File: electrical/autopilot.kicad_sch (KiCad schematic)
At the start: 5 parts

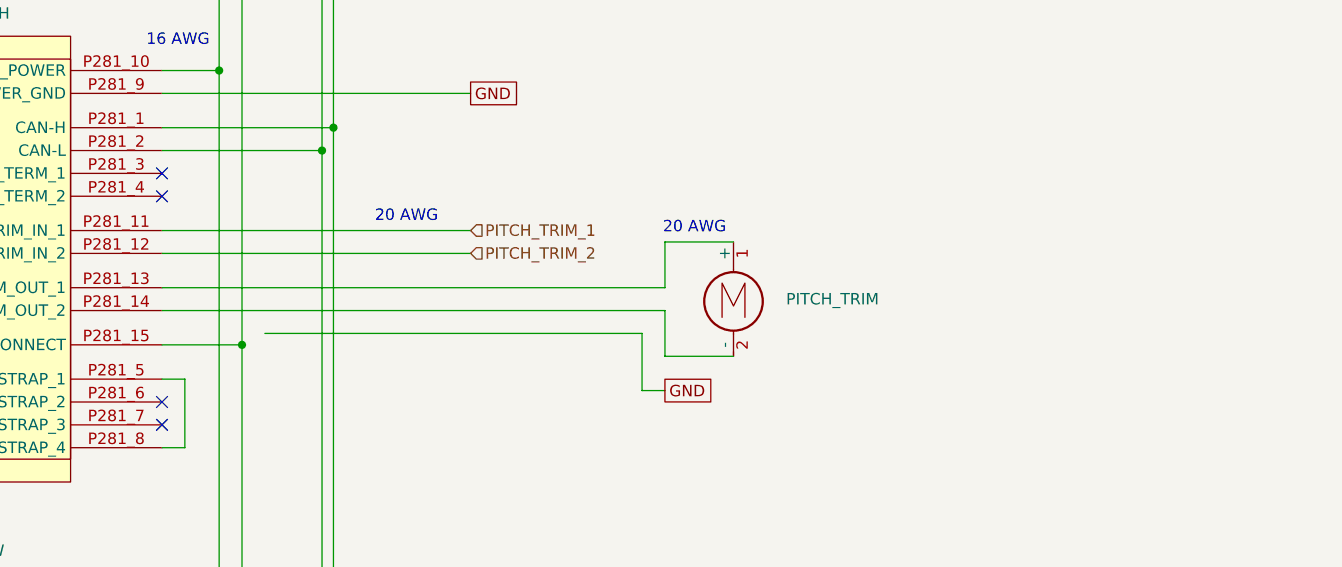
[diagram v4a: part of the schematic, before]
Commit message: Added Rudder Trim and Ray Allen T3 Servo Type.
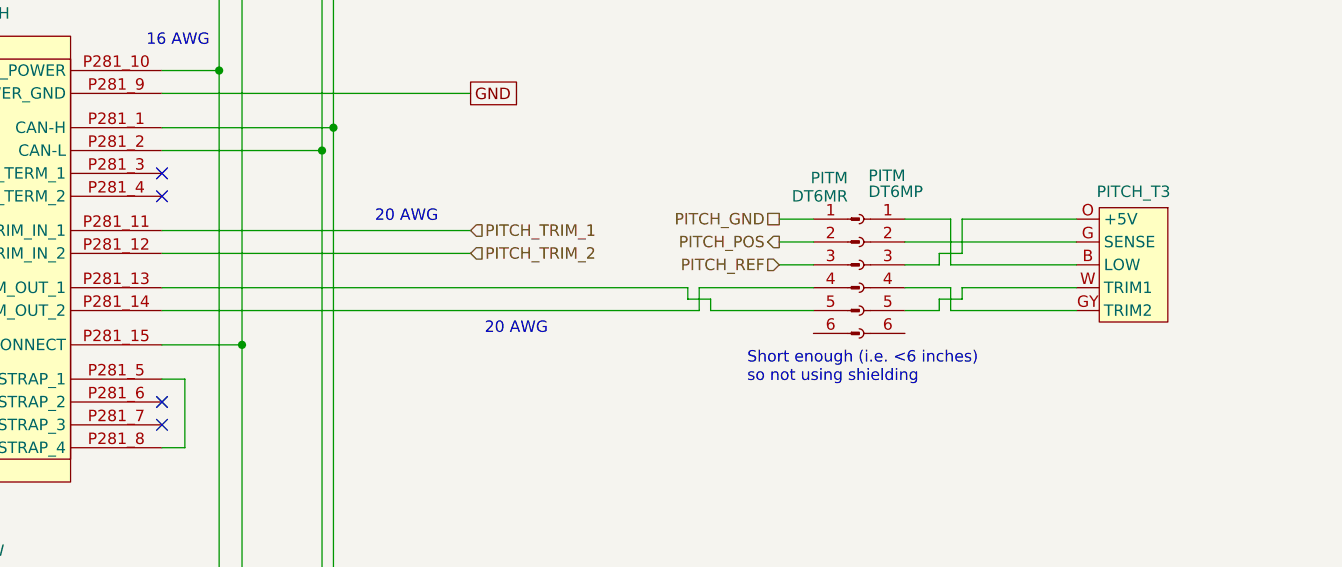
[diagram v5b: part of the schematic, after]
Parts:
- removed PITCH_TRIM: Motor_DC, symbol Motor:Motor_DC
- added PITCH_T3: ~, symbol flyerx:Ray_Allen_T2/T3
- added PITM: DT6MR, symbol Connector:Conn_01x06_Pin
- added PITM: DT6MP, symbol Connector:Conn_01x06_Socket
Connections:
- net at GSA28_PITCH.P281_13 (TRIM_OUT_1): now also PITM.5 (Pin_5)
- net at GSA28_PITCH.P281_14 (TRIM_OUT_2): now also PITM.4 (Pin_4)
- new net: PITCH_T3.B (LOW), PITM.1 (Pin_1)
- new net: PITCH_T3.G (SENSE), PITM.2 (Pin_2)
- new net: PITCH_T3.O (+5V), PITM.3 (Pin_3)
- new net: PITCH_T3.GY (TRIM2), PITM.4 (Pin_4)
- new net: PITCH_T3.W (TRIM1), PITM.5 (Pin_5)
- new net PITCH_GND: PITM.1 (Pin_1)
- new net PITCH_POS: PITM.2 (Pin_2)
- new net PITCH_REF: PITM.3 (Pin_3)
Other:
- note added: "Short enough (i.e. <6 inches) so not using shielding"

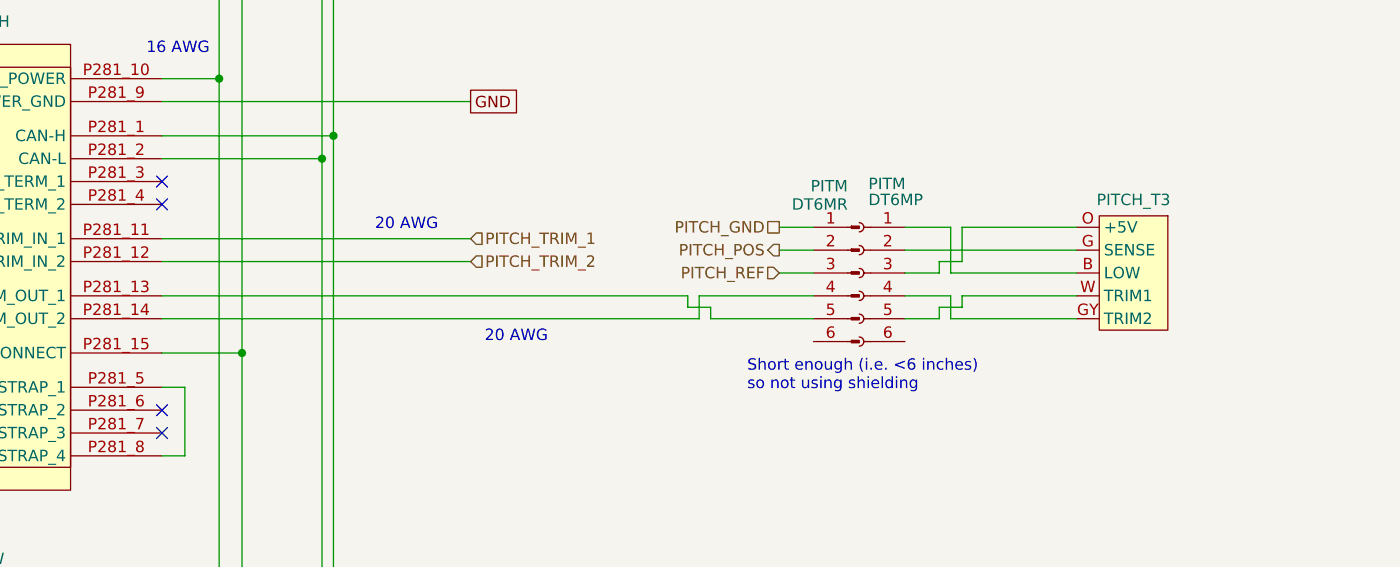
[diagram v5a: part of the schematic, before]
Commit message: Interim check-in getting colors correct.
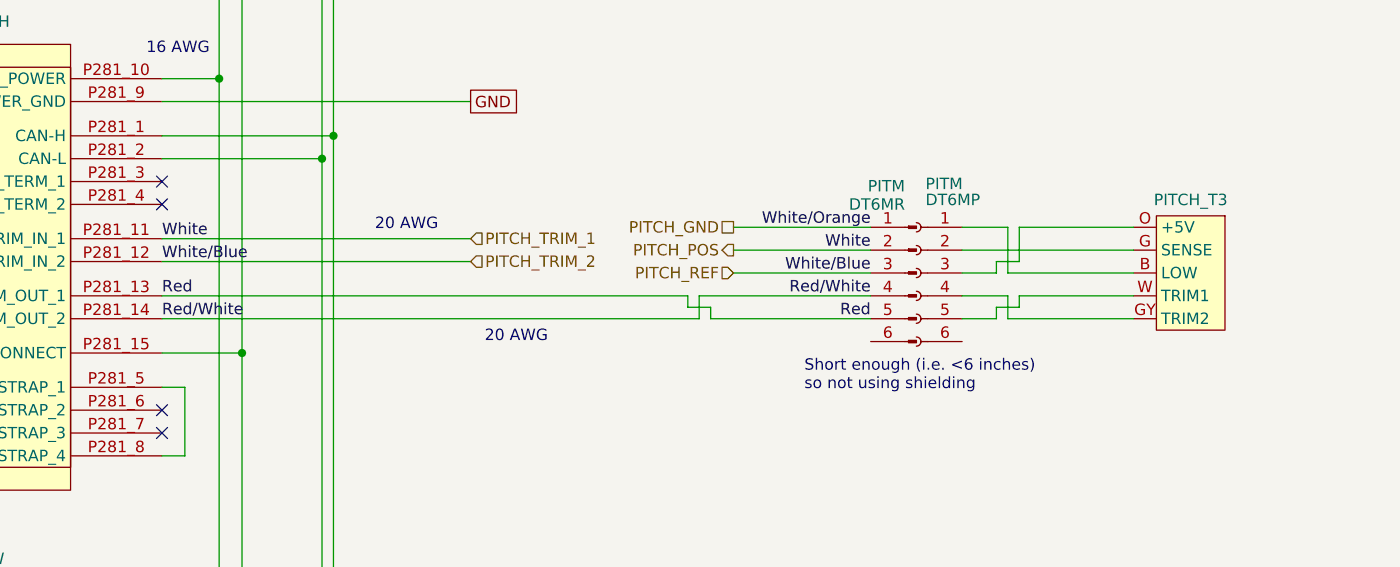
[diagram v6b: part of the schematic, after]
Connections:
- net PITCH_TRIM_1 is gone; now on net PITCH_POS: GSA28_PITCH.P281_11 (TRIM_IN_1)
- net PITCH_TRIM_2 is gone; now on net PITCH_REF: GSA28_PITCH.P281_12 (TRIM_IN_2)
- net Red/White: now reaches GSA28_PITCH.P281_14 (TRIM_OUT_2), PITM.4 (Pin_4)
- net Red: now reaches GSA28_PITCH.P281_13 (TRIM_OUT_1), PITM.5 (Pin_5)
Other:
- moved on the sheet: PITCH_T3, PITM
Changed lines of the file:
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@@
 	(text "Short enough (i.e. <6 inches)\nso not using shielding"
 		(exclude_from_sim no)
-		(at 120.904 119.38 0)
+		(at 127.254 119.38 0)
 		(effects
 			(font
@@
 	(wire
 		(pts
-			(xy 143.51 107.95) (xy 157.48 107.95)
-		)
-		(stroke
-			(width 0)
-			(type default)
-		)
-	)
-	(wire
-		(pts
-			(xy 138.43 110.49) (xy 143.51 110.49)
+			(xy 149.86 107.95) (xy 163.83 107.95)
+		)
+		(stroke
+			(width 0)
+			(type default)
+		)
+	)
+	(wire
+		(pts
+			(xy 144.78 110.49) (xy 149.86 110.49)
 		)
 		(stroke
@@
 	(wire
 		(pts
-			(xy 116.84 113.03) (xy 128.27 113.03)
+			(xy 116.84 113.03) (xy 134.62 113.03)
 		)
 		(stroke
@@
 	(wire
 		(pts
-			(xy 124.46 102.87) (xy 128.27 102.87)
+			(xy 119.38 102.87) (xy 134.62 102.87)
 		)
 		(stroke
@@
 	(wire
 		(pts
-			(xy 143.51 113.03) (xy 157.48 113.03)
+			(xy 149.86 113.03) (xy 163.83 113.03)
 		)
 		(stroke
@@
 	(wire
 		(pts
-			(xy 138.43 105.41) (xy 157.48 105.41)
+			(xy 144.78 105.41) (xy 163.83 105.41)
 		)
 		(stroke
@@
 	(wire
 		(pts
-			(xy 143.51 110.49) (xy 143.51 113.03)
+			(xy 149.86 110.49) (xy 149.86 113.03)
 		)
 		(stroke
@@
 	(wire
 		(pts
-			(xy 142.24 113.03) (xy 142.24 111.76)
+			(xy 148.59 113.03) (xy 148.59 111.76)
 		)
 		(stroke
@@
 	(wire
 		(pts
-			(xy 124.46 105.41) (xy 128.27 105.41)
-		)
-		(stroke
-			(width 0)
-			(type default)
-		)
-	)
-	(wire
-		(pts
-			(xy 144.78 111.76) (xy 144.78 110.49)
+			(xy 119.38 105.41) (xy 134.62 105.41)
+		)
+		(stroke
+			(width 0)
+			(type default)
+		)
+	)
+	(wire
+		(pts
+			(xy 151.13 111.76) (xy 151.13 110.49)
 		)
 		(stroke
@@
 	(wire
 		(pts
-			(xy 142.24 107.95) (xy 142.24 106.68)
+			(xy 148.59 107.95) (xy 148.59 106.68)
 		)
 		(stroke
@@
 	(wire
 		(pts
-			(xy 143.51 102.87) (xy 138.43 102.87)
+			(xy 149.86 102.87) (xy 144.78 102.87)
 		)
 		(stroke
@@
 	(wire
 		(pts
-			(xy 138.43 107.95) (xy 142.24 107.95)
+			(xy 144.78 107.95) (xy 148.59 107.95)
 		)
 		(stroke
@@
 	(wire
 		(pts
-			(xy 144.78 102.87) (xy 157.48 102.87)
+			(xy 151.13 102.87) (xy 163.83 102.87)
 		)
 		(stroke
@@
 	(wire
 		(pts
-			(xy 115.57 110.49) (xy 128.27 110.49)
+			(xy 115.57 110.49) (xy 134.62 110.49)
 		)
 		(stroke
@@
 	(wire
 		(pts
-			(xy 144.78 110.49) (xy 157.48 110.49)
+			(xy 151.13 110.49) (xy 163.83 110.49)
 		)
 		(stroke
@@
 	(wire
 		(pts
-			(xy 144.78 106.68) (xy 144.78 102.87)
+			(xy 151.13 106.68) (xy 151.13 102.87)
 		)
 		(stroke
@@
 	(wire
 		(pts
-			(xy 143.51 107.95) (xy 143.51 102.87)
-		)
-		(stroke
-			(width 0)
-			(type default)
-		)
-	)
-	(wire
-		(pts
-			(xy 138.43 113.03) (xy 142.24 113.03)
+			(xy 149.86 107.95) (xy 149.86 102.87)
+		)
+		(stroke
+			(width 0)
+			(type default)
+		)
+	)
+	(wire
+		(pts
+			(xy 144.78 113.03) (xy 148.59 113.03)
 		)
 		(stroke
@@
 	(wire
 		(pts
-			(xy 142.24 106.68) (xy 144.78 106.68)
+			(xy 148.59 106.68) (xy 151.13 106.68)
 		)
 		(stroke
@@
 	(wire
 		(pts
-			(xy 124.46 107.95) (xy 128.27 107.95)
-		)
-		(stroke
-			(width 0)
-			(type default)
-		)
-	)
-	(wire
-		(pts
-			(xy 142.24 111.76) (xy 144.78 111.76)
+			(xy 119.38 107.95) (xy 134.62 107.95)
+		)
+		(stroke
+			(width 0)
+			(type default)
+		)
+	)
+	(wire
+		(pts
+			(xy 148.59 111.76) (xy 151.13 111.76)
 		)
 		(stroke
@@
 			(width 0)
 			(type default)
+		)
+	)
+	(label "White{slash}Orange"
+		(at 134.62 102.87 180)
+		(effects
+			(font
+				(size 1.27 1.27)
+			)
+			(justify right bottom)
+		)
+	)
+	(label "Red"
+		(at 55.88 110.49 0)
+		(effects
+			(font
+				(size 1.27 1.27)
+			)
+			(justify left bottom)
+		)
+	)
+	(label "Red"
+		(at 134.62 113.03 180)
+		(effects
+			(font
+				(size 1.27 1.27)
+			)
+			(justify right bottom)
+		)
+	)
+	(label "Red{slash}White"
+		(at 134.62 110.49 180)
+		(effects
+			(font
+				(size 1.27 1.27)
+			)
+			(justify right bottom)
+		)
+	)
+	(label "White{slash}Blue"
+		(at 55.88 106.68 0)
+		(effects
+			(font
+				(size 1.27 1.27)
+			)
+			(justify left bottom)
+		)
+	)
+	(label "White"
+		(at 134.62 105.41 180)
+		(effects
+			(font
+				(size 1.27 1.27)
+			)
+			(justify right bottom)
+		)
+	)
+	(label "White"
+		(at 55.88 104.14 0)
+		(effects
+			(font
+				(size 1.27 1.27)
+			)
+			(justify left bottom)
+		)
+	)
+	(label "Red{slash}White"
+		(at 55.88 113.03 0)
+		(effects
+			(font
+				(size 1.27 1.27)
+			)
+			(justify left bottom)
+		)
+	)
+	(label "White{slash}Blue"
+		(at 134.62 107.95 180)
+		(effects
+			(font
+				(size 1.27 1.27)
+			)
+			(justify right bottom)
 		)
 	)
@@
 	(hierarchical_label "PITCH_REF"
 		(shape input)
-		(at 124.46 107.95 180)
+		(at 119.38 107.95 180)
 		(effects
 			(font
@@
 	(hierarchical_label "PITCH_POS"
 		(shape output)
-		(at 124.46 105.41 180)
+		(at 119.38 105.41 180)
 		(effects
 			(font
@@
 	(hierarchical_label "PITCH_GND"
 		(shape passive)
-		(at 124.46 102.87 180)
+		(at 119.38 102.87 180)
 		(effects
 			(font
@@
 	(symbol
 		(lib_id "Connector:Conn_01x06_Pin")
-		(at 133.35 107.95 0)
+		(at 139.7 107.95 0)
 		(mirror y)
 		(unit 1)
@@
 		(dnp no)
 		(property "Reference" "PITM"
-			(at 132.08 98.298 0)
+			(at 138.43 98.298 0)
 			(effects
 				(font
@@
 		)
 		(property "Value" "DT6MR"
-			(at 132.08 100.33 0)
+			(at 138.43 100.33 0)
 			(effects
 				(font
@@
 		)
 		(property "Footprint" ""
-			(at 133.35 107.95 0)
+			(at 139.7 107.95 0)
 			(effects
 				(font
@@
 		)
 		(property "Datasheet" "~"
-			(at 133.35 107.95 0)
+			(at 139.7 107.95 0)
 			(effects
 				(font
@@
 		)
 		(property "Description" "Generic connector, single row, 01x06, script generated"
-			(at 133.35 107.95 0)
+			(at 139.7 107.95 0)
 			(effects
 				(font
@@
 	(symbol
 		(lib_id "Connector:Conn_01x06_Socket")
-		(at 133.35 107.95 0)
+		(at 139.7 107.95 0)
 		(mirror y)
 		(unit 1)
@@
 		(dnp no)
 		(property "Reference" "PITM"
-			(at 134.366 98.044 0)
+			(at 140.716 98.044 0)
 			(effects
 				(font
@@
 		)
 		(property "Value" "DT6MP"
-			(at 134.366 99.822 0)
+			(at 140.716 99.822 0)
 			(effects
 				(font
@@
 		)
 		(property "Footprint" ""
-			(at 133.35 107.95 0)
+			(at 139.7 107.95 0)
 			(effects
 				(font
@@
 		)
 		(property "Datasheet" "~"
-			(at 133.35 107.95 0)
+			(at 139.7 107.95 0)
 			(effects
 				(font
@@
 		)
 		(property "Description" "Generic connector, single row, 01x06, script generated"
-			(at 133.35 107.95 0)
+			(at 139.7 107.95 0)
 			(effects
 				(font
@@
 	(symbol
 		(lib_id "flyerx:Ray_Allen_T2/T3")
-		(at 167.64 101.6 0)
+		(at 173.99 101.6 0)
 		(mirror y)
 		(unit 1)
@@
 		(dnp no)
 		(property "Reference" "PITCH_T3"
-			(at 163.83 99.822 0)
+			(at 170.18 99.822 0)
 			(effects
 				(font
@@
 		)
 		(property "Value" "~"
-			(at 163.83 99.06 0)
+			(at 170.18 99.06 0)
 			(effects
 				(font
@@
 		)
 		(property "Footprint" ""
-			(at 173.99 99.06 0)
+			(at 180.34 99.06 0)
 			(effects
 				(font
@@
 		)
 		(property "Datasheet" ""
-			(at 173.99 99.06 0)
+			(at 180.34 99.06 0)
 			(effects
 				(font
@@
 		)
 		(property "Description" ""
-			(at 167.64 101.6 0)
-			(effects
-				(font
+			(at 173.99 101.6 0)
+			(effects
+				(font
